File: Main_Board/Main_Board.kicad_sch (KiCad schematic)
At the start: 3 parts, among them U1 TCR2EF33_LMCT

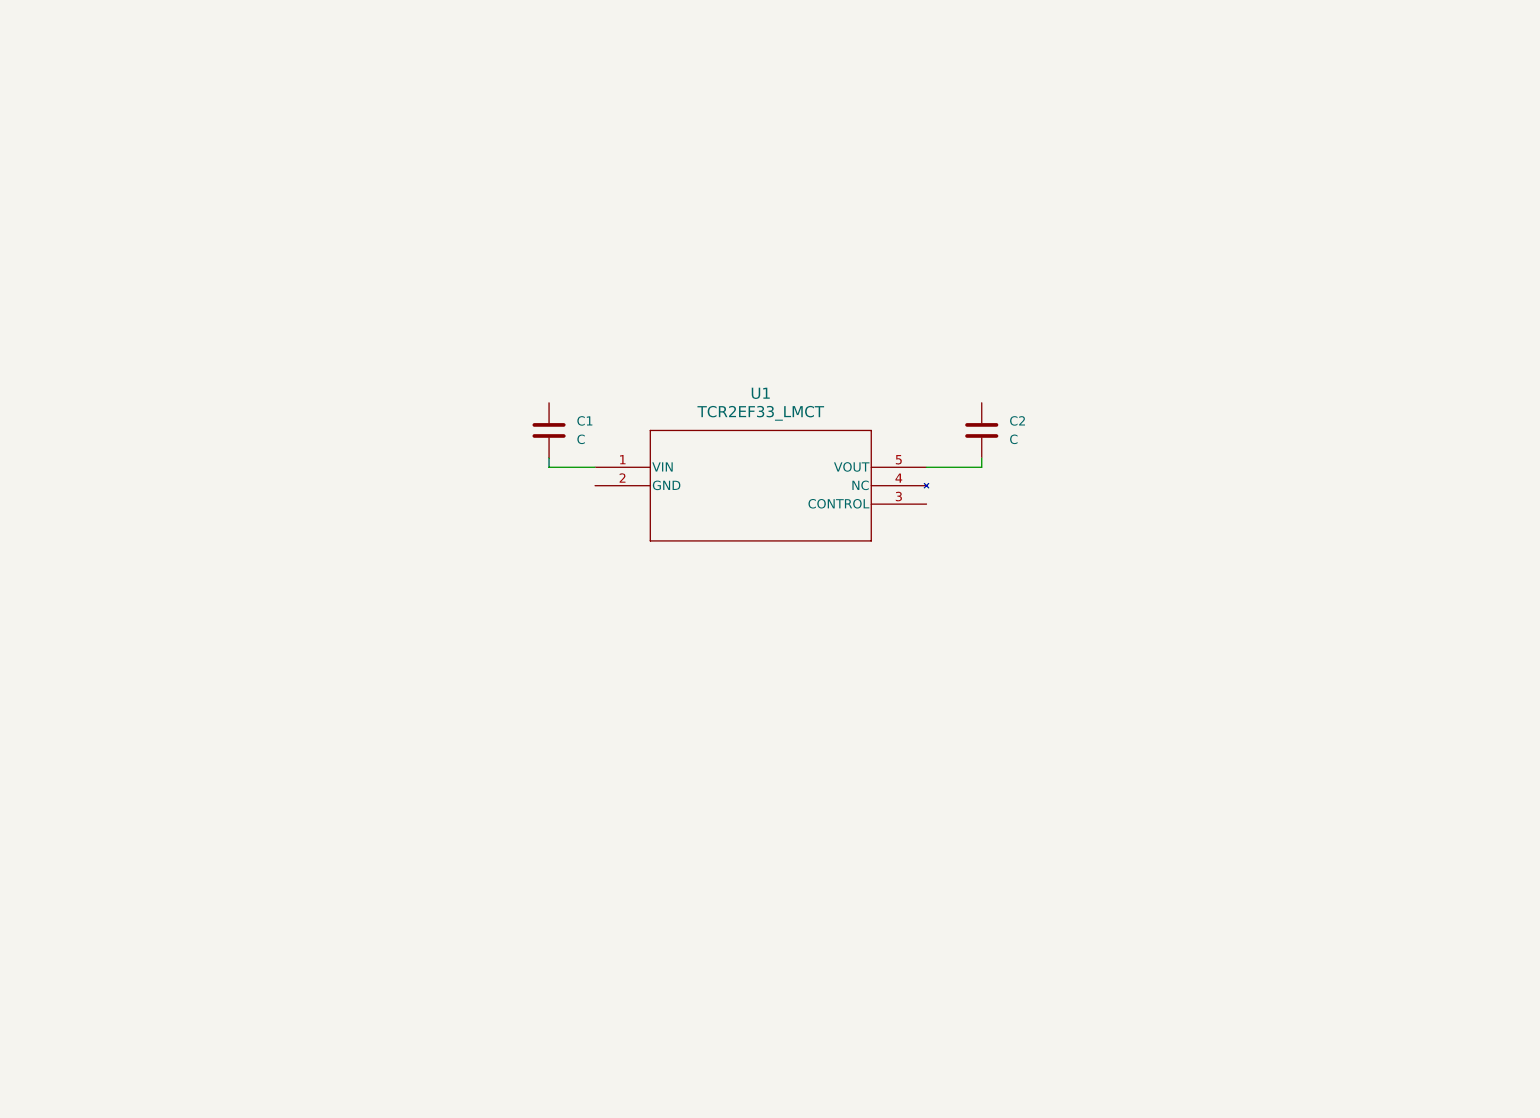
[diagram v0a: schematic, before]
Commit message: Teensy Part
Teensy part with Global Variables and also added hierarchical sheets
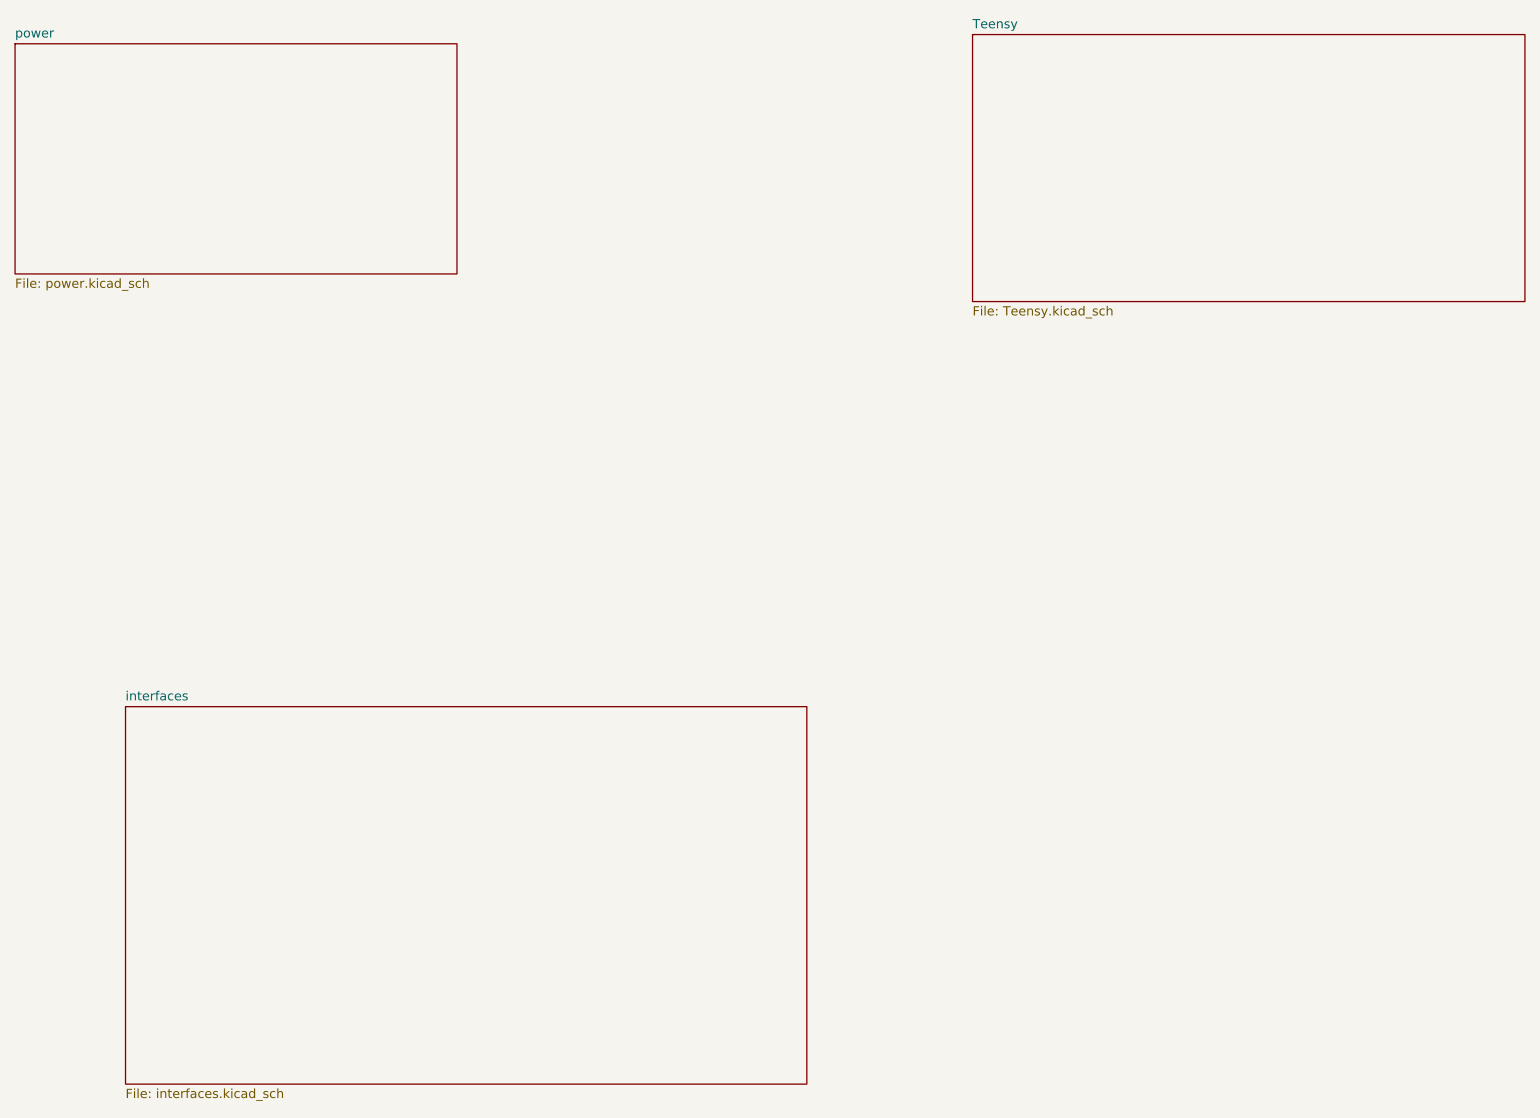
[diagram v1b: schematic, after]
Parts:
- removed C1, C2: C, Capacitor_SMD:C_1206_3216Metric_Pad1.33x1.80mm_HandSolder, symbol Device:C
- removed U1: TCR2EF33_LMCT, shared_footprints:SOT-25 SMV_TOS, symbol shared_symbols:TCR2EF33_LMCT
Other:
- added sheet Teensy (Teensy.kicad_sch)
- added sheet interfaces (interfaces.kicad_sch)
- added sheet power (power.kicad_sch)
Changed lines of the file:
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@@
 (kicad_sch
-	(version 20231120)
+	(version 20250114)
 	(generator "eeschema")
-	(generator_version "8.0")
+	(generator_version "9.0")
 	(paper "A4")
+	(sheet
+		(at 58.42 118.11)
+		(size 93.98 52.07)
+		(exclude_from_sim no)
+		(in_bom yes)
+		(on_board yes)
+		(dnp no)
+		(fields_autoplaced yes)
+		(stroke
+			(width 0.1524)
+			(type solid)
+		)
+		(fill
+			(color 0 0 0 0.0000)
+		)
+		(property "Sheetname" "interfaces"
+			(at 58.42 117.3984 0)
+			(effects
+				(font
+					(size 1.27 1.27)
+				)
+				(justify left bottom)
+			)
+		)
+		(property "Sheetfile" "interfaces.kicad_sch"
+			(at 58.42 170.7646 0)
+			(effects
+				(font
+					(size 1.27 1.27)
+				)
+				(justify left top)
+			)
+		)
+		(instances
+			(project "Main_Board"
+				(path "/a6370cae-4cc8-4463-bced-0fca34553ea8"
+					(page "4")
+				)
+			)
+		)
+	)
+	(sheet
+		(at 43.18 26.67)
+		(size 60.96 31.75)
+		(exclude_from_sim no)
+		(in_bom yes)
+		(on_board yes)
+		(dnp no)
+		(fields_autoplaced yes)
+		(stroke
+			(width 0.1524)
+			(type solid)
+		)
+		(fill
+			(color 0 0 0 0.0000)
+		)
+		(property "Sheetname" "power"
+			(at 43.18 25.9584 0)
+			(effects
+				(font
+					(size 1.27 1.27)
+				)
+				(justify left bottom)
+			)
+		)
+		(property "Sheetfile" "power.kicad_sch"
+			(at 43.18 59.0046 0)
+			(effects
+				(font
+					(size 1.27 1.27)
+				)
+				(justify left top)
+			)
+		)
+		(instances
+			(project "Main_Board"
+				(path "/a6370cae-4cc8-4463-bced-0fca34553ea8"
+					(page "2")
+				)
+			)
+		)
+	)
+	(sheet
+		(at 175.26 25.4)
+		(size 76.2 36.83)
+		(exclude_from_sim no)
+		(in_bom yes)
+		(on_board yes)
+		(dnp no)
+		(fields_autoplaced yes)
+		(stroke
+			(width 0.1524)
+			(type solid)
+		)
+		(fill
+			(color 0 0 0 0.0000)
+		)
+		(property "Sheetname" "Teensy"
+			(at 175.26 24.6884 0)
+			(effects
+				(font
+					(size 1.27 1.27)
+				)
+				(justify left bottom)
+			)
+		)
+		(property "Sheetfile" "Teensy.kicad_sch"
+			(at 175.26 62.8146 0)
+			(effects
+				(font
+					(size 1.27 1.27)
+				)
+				(justify left top)
+			)
+		)
+		(instances
+			(project "Main_Board"
+				(path "/a6370cae-4cc8-4463-bced-0fca34553ea8"
+					(page "3")
+				)
+			)
+		)
+	)
+	(sheet_instances
+		(path "/"
+			(page "1")
+		)
+	)
+	(embedded_fonts no)
+)
